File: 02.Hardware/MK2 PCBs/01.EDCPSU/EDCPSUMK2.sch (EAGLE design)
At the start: 182 parts, among them IC1 IP2721, J1 DX07S016JA1R1500, J3 AVR_ISP, J4 FTDI_DEVICE, J6 Display, K1 FLEX8, Q2 2N7002PW, Q4 2N7002PW, Q5 2N7002PW, Q9 2N7002PW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

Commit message: Revision de version definitva Javi
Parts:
- R47, R48: value (none) -> 100R
- R49: value (none) -> 10k
- R50: value (none) -> 56k
- R51: value (none) -> 220k
- R55, R56: value (none) -> 5k1
- R59: value (none) -> 1k
- R62: value (none) -> 100k
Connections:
- net GND_IN: now also J1.SHIELD
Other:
- note added: "LOW PASS FILTER Fc= 7Hz"
- note added: "Ratio= 1/5 5V @ Vi=25V"
- moved on the sheet: C55, C57, C58, D7, IN+, IN-, Q5, R48, R49, R50, R51, R55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

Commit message: Update Note 22-RTR (Ready To Revision)
Add Resistor N.A for Divisor
Connect USb Shield to GND
Fix silkcreen and Position
Fix IN_OVC to MCPU
Plane for VOUT and GND in Flex Connection
Fix Test Pint Positions
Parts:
- removed GND, PEDAL+, PEDAL-, VOUT+: TEST-POINT3, SparkFun-Connectors:TEST-POINT3
- removed TP13: M01POGOPIN_HOLE_LARGE, SparkFun-Connectors:M01POGOPIN_HOLE_LARGE
- added R34: N.A, SparkFun-Resistors:RESISTOR0603
- renumbered IC1 to U10
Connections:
- removed net TEST: TP13.1
- removed net VOUT+: TP11.1
- net GND: no longer GND.1
- net GND_IN: now also R34.1
- net IN_OVC: no longer U1.PB1(OC1A)
- net N$59: now also R34.2
- net PEDAL+: no longer PEDAL+.1
- net PEDAL-: no longer PEDAL-.1
- net VOUT: now also TP11.1; no longer VOUT+.1

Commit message: Añadido SPARE2 + revisión
Se añade SPARE2 con R y Pad para  tener un punto de acceso al pin 13 de CPU.
Pequeños cambios en revisión
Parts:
- added R38: N.A, SparkFun-Resistors:RESISTOR0603
- added TP1: M01POGOPIN_HOLE_LARGE, SparkFun-Connectors:M01POGOPIN_HOLE_LARGE
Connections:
- new net N$38: R38.2, TP1.1
- new net SPARE2: R38.1, U1.PB1(OC1A)
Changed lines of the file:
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@@
 <part name="GND58" library="SparkFun" deviceset="GND" device=""/>
 <part name="R34" library="SparkFun-Resistors" library_urn="urn:adsk.eagle:library:532" deviceset="RESISTOR" device="0603" package3d_urn="urn:adsk.eagle:package:39650/1" value="N.A"/>
+<part name="TP1" library="SparkFun-Connectors" deviceset="M01" device="POGOPIN_HOLE_LARGE" value=""/>
+<part name="R38" library="SparkFun-Resistors" library_urn="urn:adsk.eagle:library:532" deviceset="RESISTOR" device="0603" package3d_urn="urn:adsk.eagle:package:39650/1" value="N.A"/>
 </parts>
 <sheets>
@@
 <attribute name="VALUE" x="270.764" y="281.94" size="1.778" layer="96" font="vector" rot="R90" align="top-center"/>
 </instance>
+<instance part="TP1" gate="G$1" x="424.18" y="203.2" smashed="yes" rot="R270">
+<attribute name="VALUE" x="419.1" y="205.74" size="1.778" layer="96" rot="R270"/>
+<attribute name="NAME" x="427.482" y="205.74" size="1.778" layer="95" rot="R270"/>
+</instance>
+<instance part="R38" gate="G$1" x="431.8" y="193.04" smashed="yes" rot="R180">
+<attribute name="NAME" x="431.8" y="191.516" size="1.778" layer="95" font="vector" rot="R180" align="bottom-center"/>
+<attribute name="VALUE" x="431.8" y="194.564" size="1.778" layer="96" font="vector" rot="R180" align="top-center"/>
+</instance>
 </instances>
 <busses>
@@
 </segment>
 </net>
+<net name="SPARE2" class="0">
+<segment>
+<pinref part="U1" gate="G$1" pin="PB1(OC1A)"/>
+<wire x1="-134.62" y1="50.8" x2="-121.92" y2="50.8" width="0.1524" layer="91"/>
+<label x="-127" y="50.8" size="1.778" layer="95"/>
+</segment>
+<segment>
+<label x="441.96" y="193.04" size="1.778" layer="95"/>
+<wire x1="436.88" y1="193.04" x2="452.12" y2="193.04" width="0.1524" layer="91"/>
+<pinref part="R38" gate="G$1" pin="1"/>
+</segment>
+</net>
+<net name="N$38" class="0">
+<segment>
+<pinref part="TP1" gate="G$1" pin="1"/>
+<wire x1="424.18" y1="195.58" x2="424.18" y2="193.04" width="0.1524" layer="91"/>
+<pinref part="R38" gate="G$1" pin="2"/>
+<wire x1="424.18" y1="193.04" x2="426.72" y2="193.04" width="0.1524" layer="91"/>
+</segment>
+</net>

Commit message: Planos modificados
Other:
- note removed: "POSIBLE EXTIRPACION!!"
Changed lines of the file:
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@@
 Es el de G=25 (TEUK version)</text>
 <text x="269.24" y="68.58" size="1.778" layer="91">ISENSE = Iout * 0.05 * 25 = Iout * 1.25</text>
-<text x="279.4" y="-58.42" size="1.778" layer="91">POSIBLE EXTIRPACION!!</text>
 <text x="99.06" y="231.14" size="6.4516" layer="94">FLEX Connectors</text>
 <text x="-40.64" y="297.18" size="1.778" layer="91">Ratio= 1/5
@@
 </segment>
 </net>
-<net name="N$33" class="0">
-<segment>
-<wire x1="274.32" y1="-91.44" x2="340.36" y2="-91.44" width="0.1524" layer="91"/>
-<wire x1="340.36" y1="-91.44" x2="340.36" y2="-30.48" width="0.1524" layer="91"/>
-<wire x1="340.36" y1="-30.48" x2="274.32" y2="-30.48" width="0.1524" layer="91"/>
-<wire x1="274.32" y1="-30.48" x2="274.32" y2="-91.44" width="0.1524" layer="91"/>
-</segment>
-</net>

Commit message: Update PCB ECPSUMK2
Actualizacion y mejora de las capas de PWR y GND
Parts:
- TP2: value M01POGOPIN_HOLE_LARGE -> VCCIO
- TP5: value M01POGOPIN_HOLE_LARGE -> PEDAL
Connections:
- net N$31 renamed PEDAL
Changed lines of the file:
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@@
 <part name="L6" library="SparkFun" deviceset="RESISTOR" device="0805-RES" value="MMZ2012Y202BT000"/>
 <part name="C16" library="SparkFun" deviceset="CAP" device="0805" value="1uF"/>
-<part name="TP2" library="SparkFun-Connectors" deviceset="M01" device="POGOPIN_HOLE_LARGE" value=""/>
+<part name="TP2" library="SparkFun-Connectors" deviceset="M01" device="POGOPIN_HOLE_LARGE" value="VCCIO"/>
 <part name="U$15" library="microbuilder" deviceset="VCCIO" device=""/>
 <part name="TP3" library="SparkFun-Connectors" deviceset="M01" device="NOSILK-KIT" value="M01NOSILK-KIT"/>
@@
 <part name="L7" library="SparkFun" deviceset="RESISTOR" device="0805-RES" value="MMZ2012Y202BT000"/>
 <part name="P+5" library="microbuilder" deviceset="VCC" device=""/>
-<part name="TP5" library="SparkFun-Connectors" deviceset="M01" device="POGOPIN_HOLE_LARGE" value=""/>
+<part name="TP5" library="SparkFun-Connectors" deviceset="M01" device="POGOPIN_HOLE_LARGE" value="PEDAL"/>
 <part name="R99" library="SparkFun" deviceset="RESISTOR" device="0805-RES" value="33"/>
 <part name="R32" library="SparkFun" deviceset="RESISTOR" device="0805-RES" value="10k"/>
@@
 </segment>
 </net>
-<net name="N$31" class="0">
+<net name="PEDAL" class="0">
 <segment>
 <pinref part="R19" gate="G$1" pin="1"/>

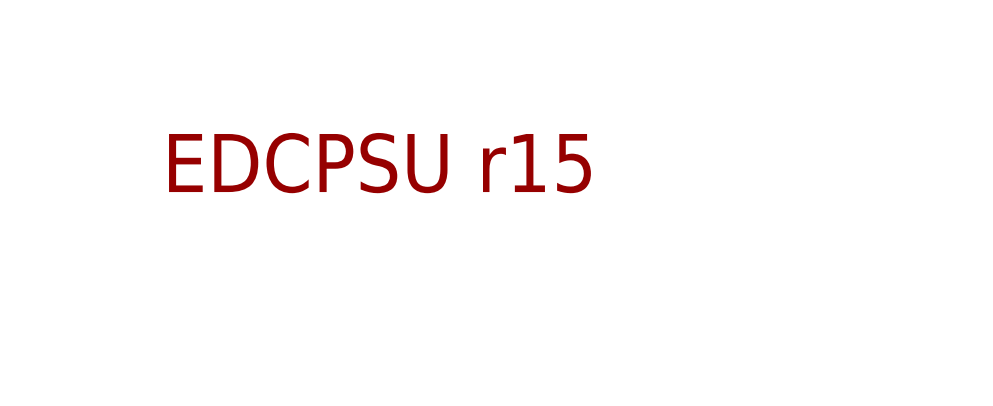
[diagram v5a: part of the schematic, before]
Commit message: Se actualiza Titulo (cajetin) a MK2 r1 mayo 22
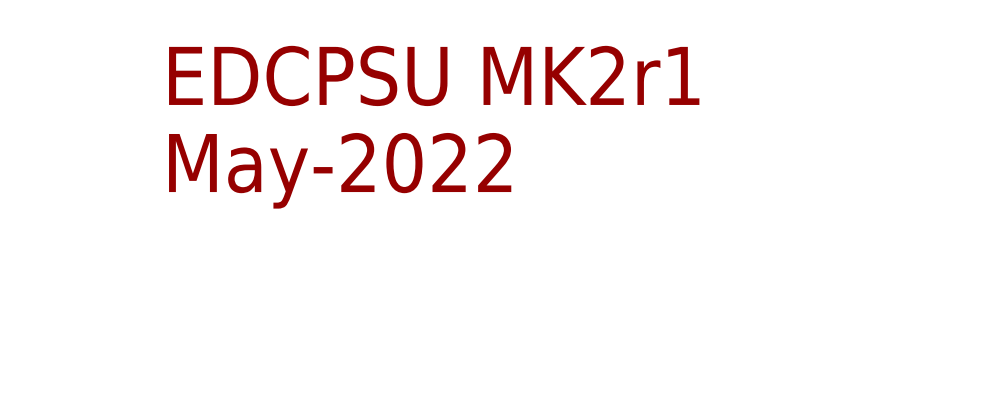
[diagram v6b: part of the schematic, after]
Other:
- note added: "EDCPSU MK2r1 May-2022"
- note removed: "EDCPSU r15"
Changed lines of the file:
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@@
 <text x="289.56" y="238.76" size="6.4516" layer="94">DIGITAL LDO + ROUTING + ISENSING</text>
 <text x="-172.72" y="111.76" size="6.4516" layer="94">MCU + USB</text>
-<text x="73.66" y="383.54" size="6.4516" layer="94">EDCPSU r15</text>
+<text x="73.66" y="383.54" size="6.4516" layer="94">EDCPSU MK2r1
+May-2022</text>
 <text x="-22.86" y="-86.36" size="1.778" layer="94">(DATA/COMMAND)</text>
 <text x="-193.04" y="-38.1" size="1.778" layer="91">Overlap buzzer assy concentric</text>
@@
 <text x="-7.62" y="-22.86" size="6.4516" layer="94">DISPLAY</text>
 <wire x1="-228.6" y1="-88.9" x2="-228.6" y2="-10.16" width="0.1524" layer="98" style="shortdash"/>
-<wire x1="-83.82" y1="408.94" x2="584.2" y2="416.56" width="0.1524" layer="98" style="shortdash"/>
+<wire x1="-106.68" y1="416.56" x2="584.2" y2="416.56" width="0.1524" layer="98" style="shortdash"/>
 <wire x1="584.2" y1="416.56" x2="571.5" y2="-33.02" width="0.1524" layer="98" style="shortdash"/>
 <wire x1="571.5" y1="-33.02" x2="571.5" y2="-86.36" width="0.1524" layer="98" style="shortdash"/>
